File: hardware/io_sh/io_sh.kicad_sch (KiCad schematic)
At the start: 25 parts, among them J1 BTB 30P socket, J11 M1+M2, J12 M3+M4, J13 M5+M6, J14 M7+M8, J15 M9+M10, J2 BTB 30P socket, J3 5V IN, J4 LED STRIP, J5 LED PWR, J6 E-STOP, J7 PANEL BTN, U1 74AHCT1G125

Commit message: Schematic review fixes from datasheet checks
- Crystal: Abracon ABM8-272-T3, which the RP2350 design guide's
  15 pF / 1k values are tuned for (the YXC part needs 20 pF load).
- Status LED: power from V5 and buffer the 3.3 V data through a
  74AHCT1G125; the diode drop left VDD below the 3.7 V minimum.
- Qwiic: drop the BAT54WS power-in path. The ME6211 conducts from
  VOUT to VIN, so a Qwiic-fed 3V3 would back-power V5.
- Notes: sense resistors chop at 0.2-0.29 A rather than fault;
  the NO_ESTOP jumper must be cut when an e-stop is fitted.
- README: AT8833 capacitor values, inductor orientation, VMOT_SENSE
  limits, and open items (V5 capacitance, e-stop masking by a held
  button, E9 reset behaviour on motor inputs).

Co-Authored-By: Claude Opus 5.5 <noreply@anthropic.com>
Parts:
- JP2: Note cut when an NC e-stop is fitted -> MUST cut when an NC e-stop is fitted, or the e-stop does no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
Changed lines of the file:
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@@
 			)
 		)
-		(property "Note" "cut when an NC e-stop is fitted"
+		(property "Note" "MUST cut when an NC e-stop is fitted, or the e-stop does nothing; silkscreen this"
 			(at 48.26 121.92 0)
 			(hide yes)

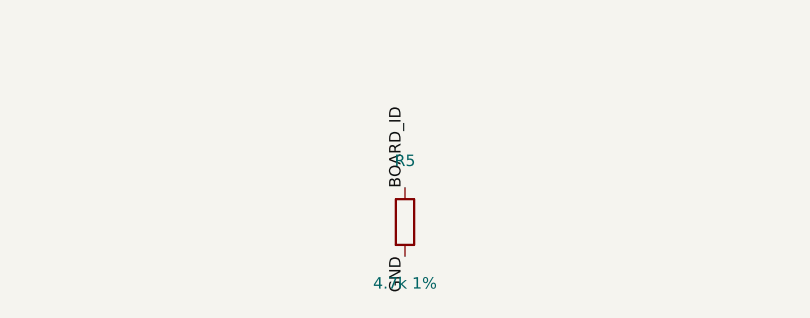
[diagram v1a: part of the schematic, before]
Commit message: Board-ID table with 5% resistors; crystal LCSC number
Eight levels from common 0402 values (0, 1k, 2.2k, 4.7k, 10k, 22k,
47k, not fitted) against the controller's 10k 1% pull-up. Worst case
with 5% ID resistors, adjacent levels stay >= 249 mV apart. io_xh
keeps 10k and io_sh 4.7k, now 5%; other rows are left free.

ABM8-272-T3 is LCSC C20625731.

Co-Authored-By: Claude Opus 5.5 <noreply@anthropic.com>
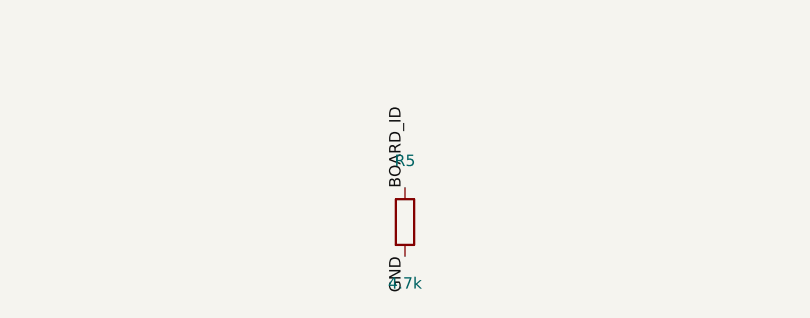
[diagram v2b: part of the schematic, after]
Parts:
- R5: value 4.7k 1% -> 4.7k; Note board-ID level; table TBD -> board-ID level; 5% ok, see hardware/README.md
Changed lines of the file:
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@@
 			)
 		)
-		(property "Value" "4.7k 1%"
+		(property "Value" "4.7k"
 			(at 302.26 131.27 0)
 			(effects
@@
 			)
 		)
-		(property "Note" "board-ID level; table TBD"
+		(property "Note" "board-ID level; 5% ok, see hardware/README.md"
 			(at 302.26 124.46 0)
 			(hide yes)

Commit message: Stack: DF40 2.0 mm connectors, 30x30 boards, controller placement
- BTB: Hirose DF40 40-pin, 2.0 mm stack (header DF40C-40DP C424643,
  socket DF40C(2.0)-40DS C597934). The 0.8 mm XUNPU stack left no room
  for parts between boards (the driver QFNs alone are 0.75-0.8 mm).
  Corner contacts are metal fittings per Hirose: tied to GND, not used
  for current. Footprints generated from the catalogue layouts; the
  header's rows are mirrored so pin n mates pin n after the flip.
- Repin: A carries M1-M7, B carries M8-M10 and the utilities, in the
  MCU's pin order so the controller's traces fan in without crossing.
  13 V5 pins across both connectors (was 6).
- Boards grow to 30 x 30 mm; controller is 4-layer, 1.0 mm thick.
- gen/pcbgen.py starts the controller PCB once: outline, stackup,
  JLCPCB rules and net classes, and a first placement of every part
  (buttons over the BTB headers, regulator by its pins, decoupling
  under the MCU). The layout is hand-edited from here.

Co-Authored-By: Claude Opus 5.5 <noreply@anthropic.com>
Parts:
- removed J2: BTB 30P socket, stack:XUNPU_BTB0.408-30P_Socket, symbol Connector_Generic:Conn_02x15_Odd_Even
- added J2: BTB 40P socket, stack:Hirose_DF40C-2.0-40DS_Socket, symbol Connector_Generic:Conn_02x20_Odd_Even
- J1: value BTB 30P socket -> BTB 40P socket; footprint stack:XUNPU_BTB0.408-30P_Socket -> stack:Hirose_DF40C-2.0-40DS_Socket; symbol Connector_Generic:Conn_02x15_Odd_Even -> Connector_Generic:Conn_02x20_Odd_Even; LCSC C42420584 -> C597934; MPN BTB0.408-30PLBDR-M41 -> DF40C(2.0)-40DS-0.4V(51)
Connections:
- net BOARD_ID: now also J2.12 (Pin_12)
- net GND: now also J1.17 (Pin_17), J1.2 (Pin_2), J1.26 (Pin_26), J1.39 (Pin_39), J1.40 (Pin_40), J1.7 (Pin_7), J1.8 (Pin_8), J2.1 (Pin_1), J2.13 (Pin_13), J2.14 (Pin_14), J2.2 (Pin_2), J2.23 (Pin_23), J2.28 (Pin_28), J2.33 (Pin_33), J2.34 (Pin_34), J2.35 (Pin_35), J2.36 (Pin_36), J2.37 (Pin_37), J2.38 (Pin_38), J2.39 (Pin_39), J2.40 (Pin_40), J2.8 (Pin_8), J2.9 (Pin_9); no longer J1.11 (Pin_11), J1.20 (Pin_20), J1.29 (Pin_29), J1.30 (Pin_30), J1.5 (Pin_5), J1.6 (Pin_6)
- net LADDER: now also J2.11 (Pin_11)
- net LED_DATA: now also J2.10 (Pin_10)
- net M10_AOUT1: now also J2.18 (Pin_18)
- net M10_AOUT2: now also J2.17 (Pin_17)
- net M10_BOUT1: now also J2.16 (Pin_16)
- net M10_BOUT2: now also J2.15 (Pin_15)
- net M1_AOUT1: now also J1.9 (Pin_9); no longer J1.7 (Pin_7)
- net M1_AOUT2: now also J1.10 (Pin_10); no longer J1.8 (Pin_8)
- net M1_BOUT1: now also J1.11 (Pin_11); no longer J1.9 (Pin_9)
- net M1_BOUT2: now also J1.12 (Pin_12); no longer J1.10 (Pin_10)
- net M2_AOUT1: now also J1.13 (Pin_13); no longer J1.12 (Pin_12)
- net M2_AOUT2: now also J1.14 (Pin_14); no longer J1.13 (Pin_13)
- net M2_BOUT1: now also J1.15 (Pin_15); no longer J1.14 (Pin_14)
- net M2_BOUT2: now also J1.16 (Pin_16); no longer J1.15 (Pin_15)
- net M3_AOUT1: now also J1.18 (Pin_18); no longer J1.16 (Pin_16)
- net M3_AOUT2: now also J1.19 (Pin_19); no longer J1.17 (Pin_17)
- net M3_BOUT1: now also J1.20 (Pin_20); no longer J1.18 (Pin_18)
- net M3_BOUT2: now also J1.21 (Pin_21); no longer J1.19 (Pin_19)
- net M4_AOUT1: now also J1.22 (Pin_22); no longer J1.21 (Pin_21)
- net M4_AOUT2: now also J1.23 (Pin_23); no longer J1.22 (Pin_22)
- net M4_BOUT1: now also J1.24 (Pin_24); no longer J1.23 (Pin_23)
- net M4_BOUT2: now also J1.25 (Pin_25); no longer J1.24 (Pin_24)
- net M5_AOUT1: now also J1.27 (Pin_27); no longer J1.25 (Pin_25)
- net M5_AOUT2: now also J1.28 (Pin_28); no longer J1.26 (Pin_26)
- net M5_BOUT1: now also J1.29 (Pin_29); no longer J1.27 (Pin_27)
- net M5_BOUT2: now also J1.30 (Pin_30); no longer J1.28 (Pin_28)
- net M6_AOUT1: now also J1.31 (Pin_31)
- net M6_AOUT2: now also J1.32 (Pin_32)
- net M6_BOUT1: now also J1.33 (Pin_33)
- net M6_BOUT2: now also J1.34 (Pin_34)
- net M7_AOUT1: now also J1.35 (Pin_35)
- net M7_AOUT2: now also J1.36 (Pin_36)
- net M7_BOUT1: now also J1.37 (Pin_37)
- net M7_BOUT2: now also J1.38 (Pin_38)
- net M8_AOUT1: now also J2.27 (Pin_27)
- net M8_AOUT2: now also J2.26 (Pin_26)
- net M8_BOUT1: now also J2.25 (Pin_25)
- net M8_BOUT2: now also J2.24 (Pin_24)
- net M9_AOUT1: now also J2.22 (Pin_22)
- net M9_AOUT2: now also J2.21 (Pin_21)
- net M9_BOUT1: now also J2.20 (Pin_20)
- net M9_BOUT2: now also J2.19 (Pin_19)
- net V5: now also J1.5 (Pin_5), J1.6 (Pin_6), J2.29 (Pin_29), J2.3 (Pin_3), J2.30 (Pin_30), J2.31 (Pin_31), J2.32 (Pin_32), J2.4 (Pin_4), J2.5 (Pin_5), J2.6 (Pin_6), J2.7 (Pin_7); no longer J1.2 (Pin_2)

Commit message: Controller: fully routed
- BTN1/BTN2 -> XUNPU TS-1088-AR02016 (C720477), stacked in the top-right
  corner with R11/R12 under them: the TS-1187A pads over the BTB headers
  blocked the connector fan-out.
- Connector B moved 2 mm down (stack still keyed by A's +2 mm offset);
  ladder/board-ID resistor column moved right, out of the M8 path.
- BTB corner contacts left unconnected (Hirose metal fittings).
- Routing: Freerouting 2.5.0 for the bulk, then a small grid router for
  the remaining nets and plane stitching. DRC: 0 unconnected, only
  silkscreen warnings and one harmless track stub left.

Co-Authored-By: Claude Opus 5.5 <noreply@anthropic.com>
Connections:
- net GND: no longer J1.1 (Pin_1), J1.2 (Pin_2), J1.39 (Pin_39), J1.40 (Pin_40), J2.1 (Pin_1), J2.2 (Pin_2), J2.39 (Pin_39), J2.40 (Pin_40)
- no-connect marks 0 -> 8
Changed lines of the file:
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@@
 		)
 	)
-	(label "GND"
-		(at 43.18 38.1 180)
-		(effects
-			(font
-				(size 1.27 1.27)
-			)
-			(justify right bottom)
-		)
-	)
-	(label "GND"
-		(at 55.88 38.1 0)
-		(effects
-			(font
-				(size 1.27 1.27)
-			)
-			(justify left bottom)
-		)
+	(no_connect
+		(at 43.18 38.1)
+	)
+	(no_connect
+		(at 55.88 38.1)
 	)
 	(label "V5"
@@
 		)
 	)
-	(label "GND"
-		(at 43.18 86.36 180)
-		(effects
-			(font
-				(size 1.27 1.27)
-			)
-			(justify right bottom)
-		)
-	)
-	(label "GND"
-		(at 55.88 86.36 0)
-		(effects
-			(font
-				(size 1.27 1.27)
-			)
-			(justify left bottom)
-		)
+	(no_connect
+		(at 43.18 86.36)
+	)
+	(no_connect
+		(at 55.88 86.36)
 	)
 	(symbol
@@
 		)
 	)
-	(label "GND"
-		(at 104.14 38.1 180)
-		(effects
-			(font
-				(size 1.27 1.27)
-			)
-			(justify right bottom)
-		)
-	)
-	(label "GND"
-		(at 116.84 38.1 0)
-		(effects
-			(font
-				(size 1.27 1.27)
-			)
-			(justify left bottom)
-		)
+	(no_connect
+		(at 104.14 38.1)
+	)
+	(no_connect
+		(at 116.84 38.1)
 	)
 	(label "V5"
@@
 		)
 	)
-	(label "GND"
-		(at 104.14 86.36 180)
-		(effects
-			(font
-				(size 1.27 1.27)
-			)
-			(justify right bottom)
-		)
-	)
-	(label "GND"
-		(at 116.84 86.36 0)
-		(effects
-			(font
-				(size 1.27 1.27)
-			)
-			(justify left bottom)
-		)
+	(no_connect
+		(at 104.14 86.36)
+	)
+	(no_connect
+		(at 116.84 86.36)
 	)
 	(symbol

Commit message: single_sh: routed single-board PCB; BOM scrub
New single-board versions of the circuit (controller + driver + IO variant
on one PCB, BTBs removed): single_sh and single_xh schematics from single()
in gen/build.py. single_sh also gets a routed board:

- 122 x 20 mm, 4 layers, 1.6 mm, all parts on top. In1 GND; In2 V5 with a
  3V3 island under the MCU (thin finger to the LDO); F/B signals.
- Along the board: USB-C + power | drivers M4-M1 | MCU | drivers M10-M5 |
  LED strip. Motor connectors J12 J11 | J15 J14 J13 so each bus leaves the
  MCU in pin order; misc connectors along the other long edge.
- Driver cells pre-routed (A1/A2 cross B1/B2 on In2 jumpers), core
  regulator copied from the controller, rest Freerouting 2.5.0 + a small
  grid router. V5 via clusters at the FET, ext-5V diode and strip fuse.
- DRC: 0 errors, 0 unconnected, schematic parity clean; 24 silkscreen
  warnings (footprint outlines).
- gen/pcbgen.py: build() split out of main(), per-board size/thickness,
  polygon zones, single_sh() placement (reproduces the routed board).

BOOTSEL on the single boards is now the TS-1088-AR02016 (C720477), same as
BTN1/BTN2; the stacked controller keeps its TS-1187A.

BOM scrub (all boards; numbers checked against the JLCPCB library):
- Every passive gets LCSC/MPN (PASSIVES in gen/build.py), basic where one
  exists. VM caps now 16 V (basic 2.2 uF is 6.3 V).
- Polyfuse C702823 (not in JLCPCB's library) -> C209721, same rating.
- Status LED C965555 (1 in stock) -> XL-2020RGBC-WS2812B C5349955, same
  pinout and footprint.
- J8 B3B-PH-K-S gets C131339.
- Solder jumpers and test pads excluded from BOM and placement files
  (schgen in_bom support; pcbgen follows the symbol).
- Schematics and *_bom.csv regenerated; controller PCB fields/attributes
  synced (layout unchanged).

Co-Authored-By: Claude Opus 5.5 <noreply@anthropic.com>
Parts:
- C1: LCSC (none) -> C52923; MPN (none) -> CL05A105KA5NQNC
- C2: LCSC (none) -> C1525; MPN (none) -> CL05B104KO5NNNC
- C3: LCSC (none) -> C15850; MPN (none) -> CL21A106KAYNNNE
- F1: LCSC C702823 -> C209721; MPN SMD1812P150TF -> SMD1812P150TF/8; Note (none) -> PTTC; 1.5 A hold / 3 A trip, 8 V
- J7: LCSC (none) -> C131339
- JP1, JP2: now left out of the parts list
- R1: LCSC (none) -> C25105; MPN (none) -> 0402WGF330JTCE
- R2: LCSC (none) -> C25765; MPN (none) -> 0402WGF2002TCE
- R3: LCSC (none) -> C25744; MPN (none) -> 0402WGF1002TCE
- R4: LCSC (none) -> C25890; MPN (none) -> 0402WGF3301TCE
- R5: LCSC (none) -> C25900; MPN (none) -> 0402WGF4701TCE
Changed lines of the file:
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@@
+			)
+		)
+		(property "LCSC" "C52923"
+			(at 525.78 40.64 0)
+			(hide yes)
+			(effects
+				(font
+					(size 1.27 1.27)
+				)
+			)
+		)
+		(property "MPN" "CL05A105KA5NQNC"
+			(at 525.78 40.64 0)
+			(hide yes)
+			(effects
+				(font
+					(size 1.27 1.27)
+				)
 			)
 		)
@@
 			)
 		)
+		(property "LCSC" "C1525"
+			(at 119.38 104.14 0)
+			(hide yes)
+			(effects
+				(font
+					(size 1.27 1.27)
+				)
+			)
+		)
+		(property "MPN" "CL05B104KO5NNNC"
+			(at 119.38 104.14 0)
+			(hide yes)
+			(effects
+				(font
+					(size 1.27 1.27)
+				)
+			)
+		)
 		(instances
 			(project "io_sh"
@@
 			)
 		)
+		(property "LCSC" "C25105"
+			(at 170.18 104.14 0)
+			(hide yes)
+			(effects
+				(font
+					(size 1.27 1.27)
+				)
+			)
+		)
+		(property "MPN" "0402WGF330JTCE"
+			(at 170.18 104.14 0)
+			(hide yes)
+			(effects
+				(font
+					(size 1.27 1.27)
+				)
+			)
+		)
 		(instances
 			(project "io_sh"
@@
 			)
 		)
-		(property "MPN" "SMD1812P150TF"
+		(property "MPN" "SMD1812P150TF/8"
 			(at 220.98 104.14 0)
 			(hide yes)
@@
 			)
 		)
-		(property "LCSC" "C702823"
+		(property "LCSC" "C209721"
+			(at 220.98 104.14 0)
+			(hide yes)
+			(effects
+				(font
+					(size 1.27 1.27)
+				)
+			)
+		)
+		(property "Note" "PTTC; 1.5 A hold / 3 A trip, 8 V"
 			(at 220.98 104.14 0)
 			(hide yes)
@@
 		(unit 1)
 		(exclude_from_sim no)
-		(in_bom yes)
+		(in_bom no)
 		(on_board yes)
 		(dnp no)
@@
 			)
 		)
+		(property "LCSC" "C15850"
+			(at 429.26 104.14 0)
+			(hide yes)
+			(effects
+				(font
+					(size 1.27 1.27)
+				)
+			)
+		)
+		(property "MPN" "CL21A106KAYNNNE"
+			(at 429.26 104.14 0)
+			(hide yes)
+			(effects
+				(font
+					(size 1.27 1.27)
+				)
+			)
+		)
 		(instances
 			(project "io_sh"
@@
 		(unit 1)
 		(exclude_from_sim no)
-		(in_bom yes)
+		(in_bom no)
 		(on_board yes)
 		(dnp no)
@@
 			)
 		)
+		(property "LCSC" "C25765"
+			(at 101.6 137.16 0)
+			(hide yes)
+			(effects
+				(font
+					(size 1.27 1.27)
+				)
+			)
+		)
+		(property "MPN" "0402WGF2002TCE"
+			(at 101.6 137.16 0)
+			(hide yes)
+			(effects
+				(font
+					(size 1.27 1.27)
+				)
+			)
+		)
 		(instances
 			(project "io_sh"
@@
 			)
 		)
+		(property "LCSC" "C131339"
+			(at 157.48 137.16 0)
+			(hide yes)
+			(effects
+				(font
+					(size 1.27 1.27)
+				)
+			)
+		)
 		(property "MPN" "B3B-PH-K-S"
 			(at 157.48 137.16 0)
@@
 			)
 		)
+		(property "LCSC" "C25744"
+			(at 203.2 137.16 0)
+			(hide yes)
+			(effects
+				(font
+					(size 1.27 1.27)
+				)
+			)
+		)
+		(property "MPN" "0402WGF1002TCE"
+			(at 203.2 137.16 0)
+			(hide yes)
+			(effects
+				(font
+					(size 1.27 1.27)
+				)
+			)
+		)
 		(instances
 			(project "io_sh"
@@
 			)
 		)
+		(property "LCSC" "C25890"
+			(at 251.46 137.16 0)
+			(hide yes)
+			(effects
+				(font
+					(size 1.27 1.27)
+				)
+			)
+		)
+		(property "MPN" "0402WGF3301TCE"
+			(at 251.46 137.16 0)
+			(hide yes)
+			(effects
+				(font
+					(size 1.27 1.27)
+				)
+			)
+		)
 		(instances
 			(project "io_sh"
@@
 			(at 302.26 137.16 0)
 			(hide yes)
+			(effects
+				(font
+					(size 1.27 1.27)
+				)
+			)
+		)
+		(property "LCSC" "C25900"
+			(at 302.26 137.16 0)
+			(hide yes)
+			(effects
+				(font
+					(size 1.27 1.27)
+				)
+			)
+		)
+		(property "MPN" "0402WGF4701TCE"
+			(at 302.26 137.16 0)
+			(hide yes)
